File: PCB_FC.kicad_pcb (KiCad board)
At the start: 2 copper layers, 20 parts, among them IC1 STM32F405RGT6, IC2 ICM-42670-P, U1 BMP388, U2 AMS1117-3.3, Y1 X32258MOB4SI

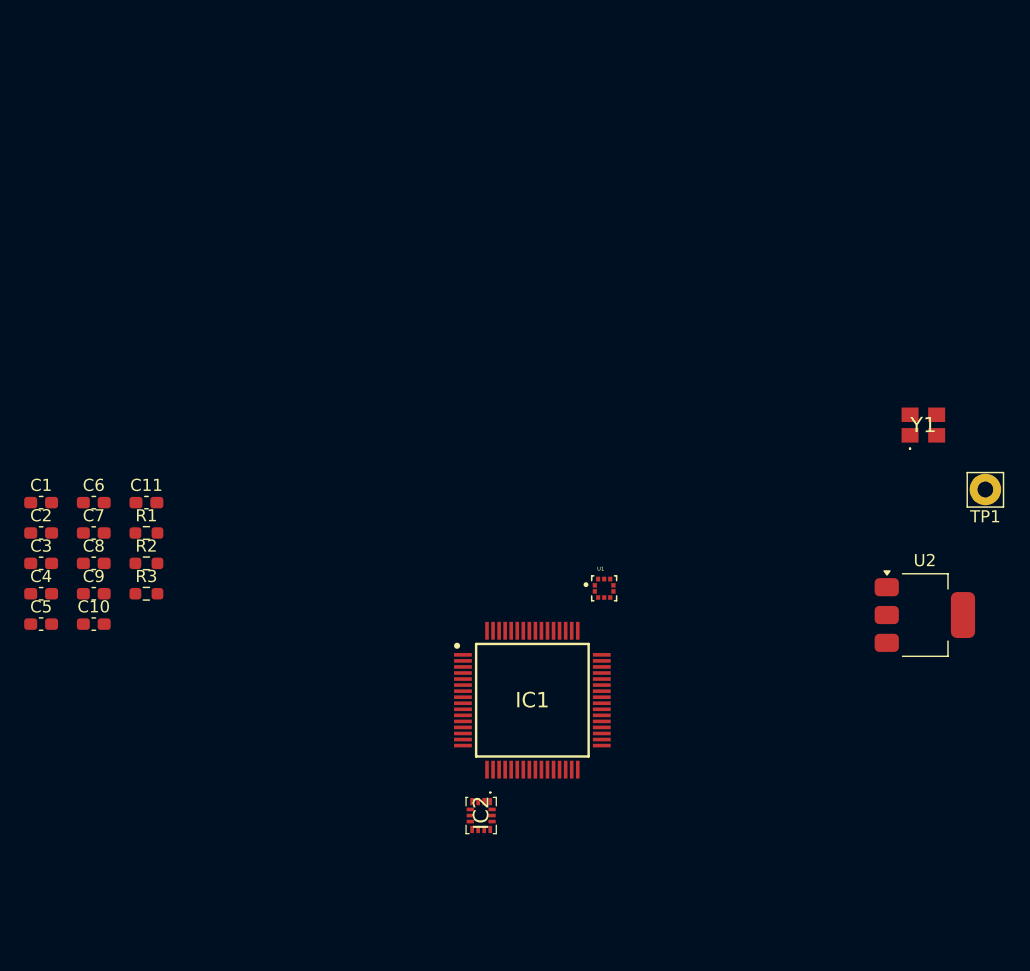
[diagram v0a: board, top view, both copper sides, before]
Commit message: Basic design of schametic done
1. Added folder for library
2. Added USB with termination resistors
3. Added Resistor network for bootstrapping and NRST
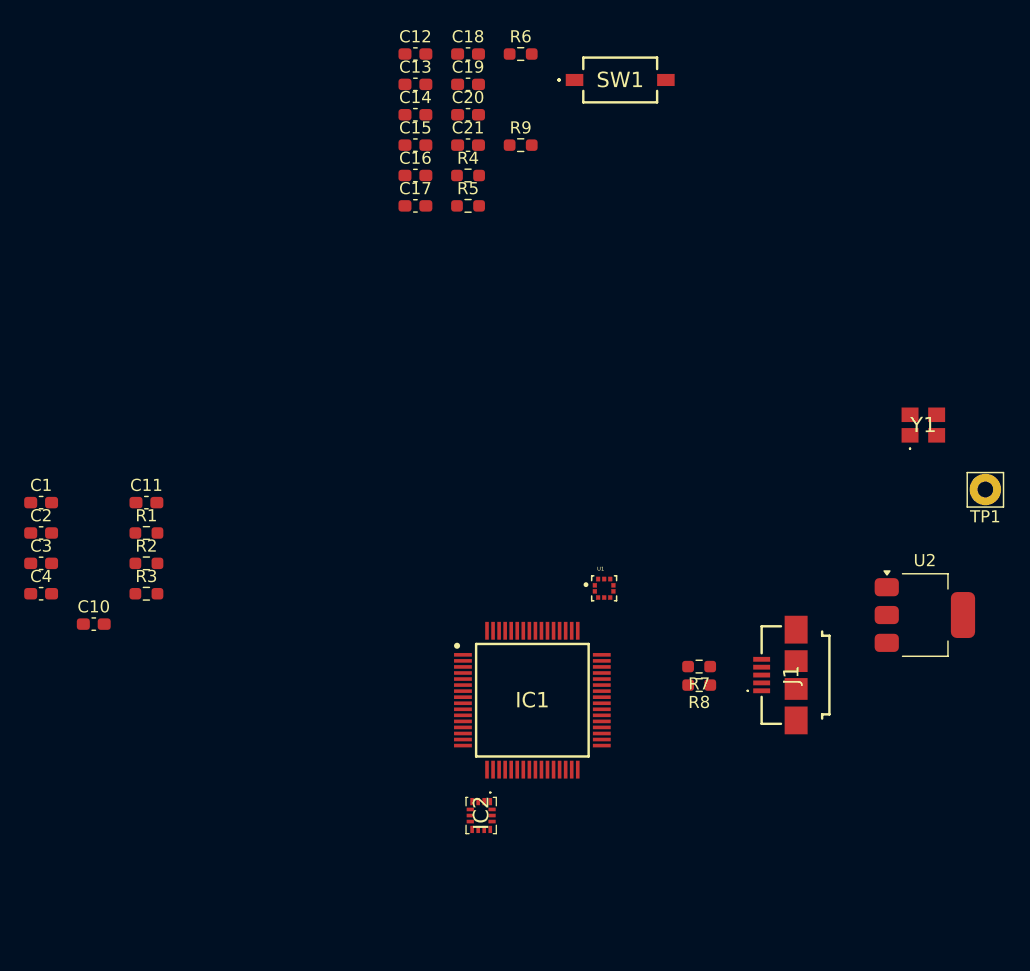
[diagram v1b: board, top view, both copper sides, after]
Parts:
- removed C5, C6: 10pF, Capacitor_SMD:C_0603_1608Metric_Pad1.08x0.95mm_HandSolder
- removed C7, C8, C9: C, Capacitor_SMD:C_0603_1608Metric_Pad1.08x0.95mm_HandSolder
- added C12: 100nf, Capacitor_SMD:C_0603_1608Metric_Pad1.08x0.95mm_HandSolder, F.Cu at (132.8, 47.0)
- added C13: 10uf, Capacitor_SMD:C_0603_1608Metric_Pad1.08x0.95mm_HandSolder, F.Cu at (132.8, 49.5)
- added C14: 10uf, Capacitor_SMD:C_0603_1608Metric_Pad1.08x0.95mm_HandSolder, F.Cu at (132.8, 52.0)
- added C15: 100nf, Capacitor_SMD:C_0603_1608Metric_Pad1.08x0.95mm_HandSolder, F.Cu at (132.8, 54.5)
- added C16: 100nf, Capacitor_SMD:C_0603_1608Metric_Pad1.08x0.95mm_HandSolder, F.Cu at (132.8, 57.0)
- added C17: 100nf, Capacitor_SMD:C_0603_1608Metric_Pad1.08x0.95mm_HandSolder, F.Cu at (132.8, 59.5)
- added C18: 100nf, Capacitor_SMD:C_0603_1608Metric_Pad1.08x0.95mm_HandSolder, F.Cu at (137.1, 47.0)
- added C19: 100nf, Capacitor_SMD:C_0603_1608Metric_Pad1.08x0.95mm_HandSolder, F.Cu at (137.1, 49.5)
- added C20: 100nf, Capacitor_SMD:C_0603_1608Metric_Pad1.08x0.95mm_HandSolder, F.Cu at (137.1, 52.0)
- added C21: 100nf, Capacitor_SMD:C_0603_1608Metric_Pad1.08x0.95mm_HandSolder, F.Cu at (137.1, 54.5)
- added J1: 10104111-0001LF, Footprint:10104111-0001LF, F.Cu at (164.2, 98.3)
- added R4: 4.7k, Resistor_SMD:R_0603_1608Metric_Pad0.98x0.95mm_HandSolder, F.Cu at (137.1, 57.0)
- added R5: 10K, Resistor_SMD:R_0603_1608Metric_Pad0.98x0.95mm_HandSolder, F.Cu at (137.1, 59.5)
- added R6: 10k, Resistor_SMD:R_0603_1608Metric_Pad0.98x0.95mm_HandSolder, F.Cu at (141.5, 47.0)
- added R7: 22R, Resistor_SMD:R_0603_1608Metric_Pad0.98x0.95mm_HandSolder, F.Cu at (156.2, 97.6)
- added R8: 22R, Resistor_SMD:R_0603_1608Metric_Pad0.98x0.95mm_HandSolder, F.Cu at (156.2, 99.2)
- added R9: 1k, Resistor_SMD:R_0603_1608Metric_Pad0.98x0.95mm_HandSolder, F.Cu at (141.5, 54.5)
- added SW1: SW_SPST, Footprint:PTS636SKG25JSMTRLFS, F.Cu at (149.7, 49.1)
- IC1: footprint KiCad:QFP50P1200X1200X160-64N -> Footprint:STM32F405RGT6
- IC2: footprint ICM-42670:ICM42670P -> Footprint:ICM-42670-P
- U1: footprint BMP388:PQFN50P200X200X80-10N -> Footprint:BMP388
- Y1: footprint X225:X32258MOB4SI -> Footprint:X32258MOB4SI
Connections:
- C1 pad 1: /3V3 -> +3.3V
- C1 pad 2: /GND -> GND
- C10 pad 2: /GND -> GND
- C11 pad 2: /GND -> GND
- C2 pad 1: /3V3 -> +3.3V
- C2 pad 2: /GND -> GND
- C3 pad 1: /3V3 -> +3.3V
- C3 pad 2: /GND -> GND
- C4 pad 1: /3V3 -> +3.3V
- C4 pad 2: /GND -> GND
- IC1 pad 12: /GND -> GND
- IC1 pad 13: /VDD -> +3.3V
- IC1 pad 18: /GND -> GND
- IC1 pad 19: /VDD -> +3.3V
- IC1 pad 32: /VDD -> +3.3V
- IC1 pad 44: / OTG_FS_DM -> /OTG_FS_D-
- IC1 pad 45: /OTG_FS_DP -> /OTG_FS_D+
- IC1 pad 46: unconnected-(IC1-PA13-Pad46) -> /SWDIO
- IC1 pad 48: /VDD -> +3.3V
- IC1 pad 49: unconnected-(IC1-PA14-Pad49) -> /SWCLK
- IC1 pad 6: Net-(IC1-PH1) -> /RCC_OUT
- IC1 pad 60: unconnected-(IC1-BOOT0-Pad60) -> Net-(IC1-BOOT0)
- IC1 pad 63: /GND -> GND
- IC1 pad 64: /VDD -> +3.3V
- IC1 pad 7: unconnected-(IC1-NRST-Pad7) -> /NRST
- IC2 pad 5: /3V3 -> +3.3V
- IC2 pad 6: /GND -> unconnected-(IC2-GND-Pad6)
- IC2 pad 8: /3V3 -> +3.3V
- R1 pad 1: /I2C2_SCL -> +3.3V
- R1 pad 2: /3V3 -> /I2C2_SCL
- R2 pad 1: /I2C2_SDA -> +3.3V
- R2 pad 2: /3V3 -> Net-(U1-CSB)
- R3 pad 1: /RCC_OUT -> Net-(Y1-CRYSTAL_1)
- R3 pad 2: Net-(IC1-PH1) -> /RCC_OUT
- U1 pad 1: /3V3 -> +3.3V
- U1 pad 10: /3V3 -> +3.3V
- U1 pad 3: /GND -> GND
- U1 pad 5: /GND -> GND
- U1 pad 6: /PAD -> Net-(U1-CSB)
- U1 pad 8: /GND -> GND
- U1 pad 9: /GND -> GND
- U2 pad 1: /GND -> GND
- U2 pad 2: /3V3 -> +3.3V
- Y1 pad 1: /RCC_IN -> Net-(Y1-CRYSTAL_1)
- Y1 pad 2: unconnected-(Y1-GND_1-Pad2) -> GND
- Y1 pad 3: unconnected-(Y1-CRYSTAL_2-Pad3) -> /RCC_IN
- Y1 pad 4: /GND -> GND

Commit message: Signal routing done
1. Routing for IMU
2. Differentially route pair for USB with termination resistor.
3. HSE crystal oscillator added.
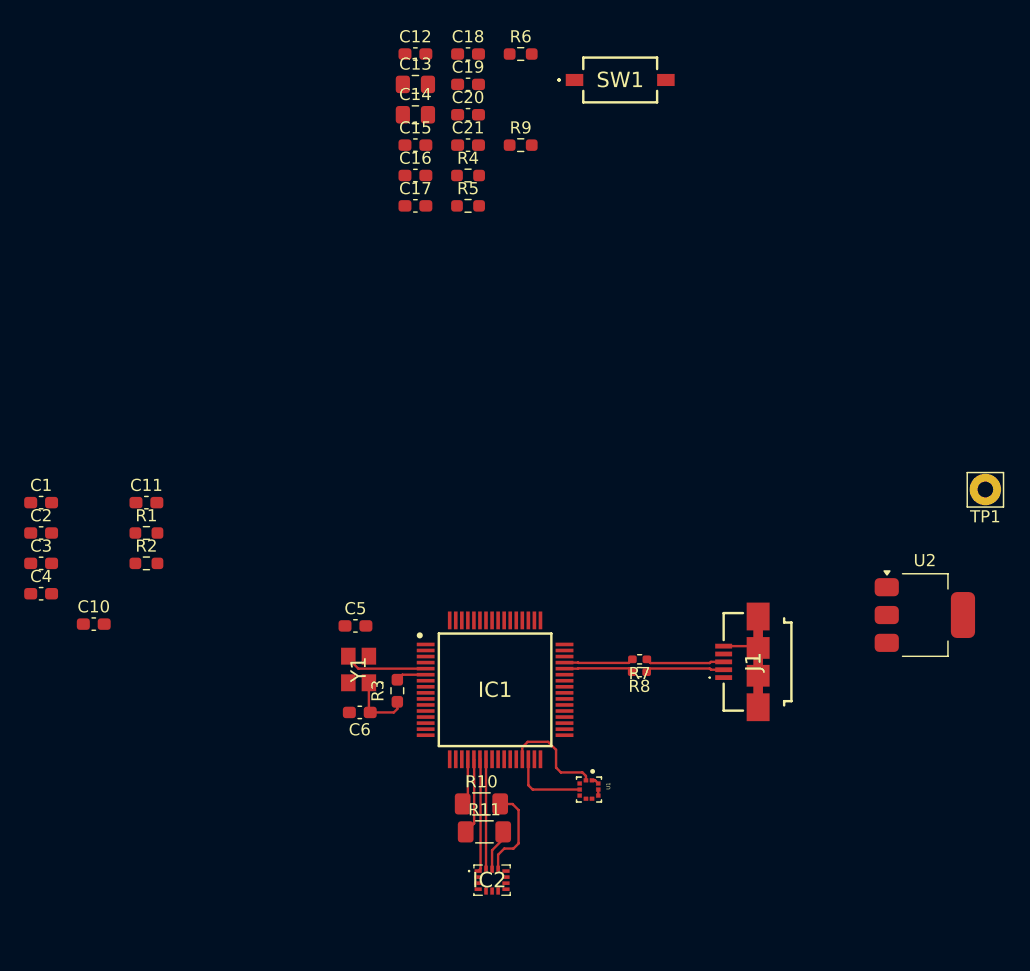
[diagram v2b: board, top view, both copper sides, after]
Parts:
- added C5: C, Capacitor_SMD:C_0603_1608Metric_Pad1.08x0.95mm_HandSolder, F.Cu at (127.8, 94.3)
- added C6: C, Capacitor_SMD:C_0603_1608Metric_Pad1.08x0.95mm_HandSolder, F.Cu at (128.2, 101.4)
- added R10: R, Resistor_SMD:R_1206_3216Metric_Pad1.30x1.75mm_HandSolder, F.Cu at (138.2, 109.0)
- added R11: R, Resistor_SMD:R_1206_3216Metric_Pad1.30x1.75mm_HandSolder, F.Cu at (138.5, 111.3)
- C13, C14: footprint Capacitor_SMD:C_0603_1608Metric_Pad1.08x0.95mm_HandSolder -> Capacitor_SMD:C_0805_2012Metric_Pad1.18x1.45mm_HandSolder
- R7, R8: footprint Resistor_SMD:R_0603_1608Metric_Pad0.98x0.95mm_HandSolder -> Resistor_SMD:R_0402_1005Metric_Pad0.72x0.64mm_HandSolder
- moved Y1 50.9 mm to (128.1, 97.9), turned to 90 degrees
- moved R3 22.2 mm to (131.3, 99.6), turned to 90 degrees
- moved U1 16.7 mm to (147.1, 107.8), turned to -90 degrees
- moved IC2 5.42 mm to (139.1, 115.3), turned to 0 degrees
- moved R8 5.06 mm to (151.3, 98.1)
- moved R7 4.95 mm to (151.3, 97.0)
- moved J1 3.32 mm to (161.1, 97.2)
- moved IC1 3.20 mm to (139.4, 99.5)
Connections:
- IC2 pad 12: /SPI1_CS -> Net-(IC2-AP_CS)
- IC2 pad 13: /SPI1_SCK SPI1 -> Net-(IC2-AP_SCL_/_AP_SCLK)
- IC2 pad 6: unconnected-(IC2-GND-Pad6) -> GND
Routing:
- net GND: track 0.00 -> 10.9 mm
- net /SPI1_MISO SPI1: track 0.00 -> 9.34 mm
- net /SPI1_MOSI SPI1: track 0.00 -> 9.09 mm
- net /I2C2_SCL: track 0.00 -> 8.82 mm
- net Net-(IC2-AP_CS): track 0.00 -> 7.51 mm
- net /RCC_IN: track 0.00 -> 6.94 mm
- net /I2C2_SDA: track 0.00 -> 6.54 mm
- net /D+: track 0.00 -> 6.52 mm
- net /D-: track 0.00 -> 6.50 mm
- net /SPI1_SCK SPI1: track 0.00 -> 6.30 mm
- net /OTG_FS_D+: track 0.00 -> 5.74 mm
- net /OTG_FS_D-: track 0.00 -> 5.71 mm
- net Net-(Y1-CRYSTAL_1): track 0.00 -> 5.44 mm
- net /SPI1_CS: track 0.00 -> 3.87 mm
- net Net-(IC2-AP_SCL_/_AP_SCLK): track 0.00 -> 3.47 mm
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
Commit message: PCB complete add logos
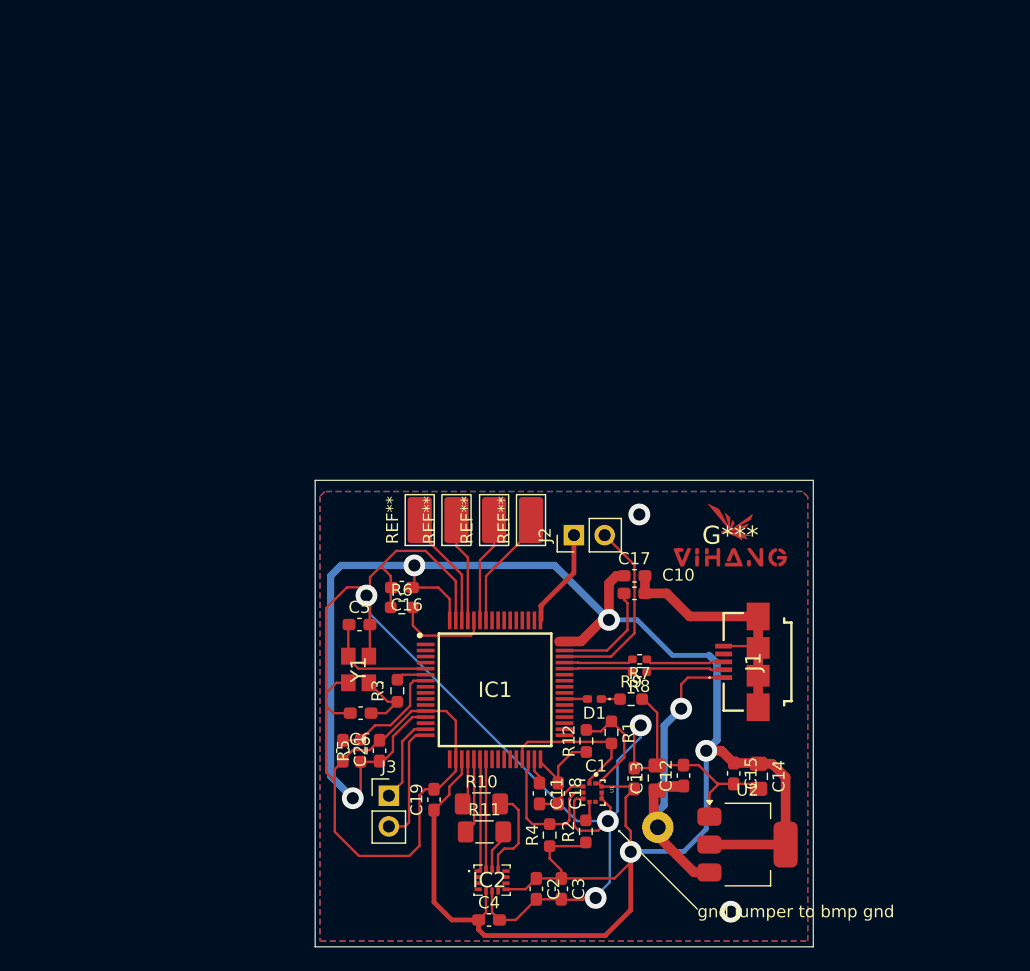
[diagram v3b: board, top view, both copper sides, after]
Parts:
- removed SW1: SW_SPST, Footprint:PTS636SKG25JSMTRLFS
- added D1: LED, LED_SMD:LED_0402_1005Metric_Pad0.77x0.64mm_HandSolder, F.Cu at (147.6, 100.3)
- added G***: LOGO, LOGO, F.Cu at (158.8, 86.8)
- added J2: Conn_01x02, Connector_PinHeader_2.54mm:PinHeader_1x02_P2.54mm_Vertical, F.Cu at (145.9, 86.8)
- added J3: Conn_01x02, Connector_PinHeader_2.54mm:PinHeader_1x02_P2.54mm_Vertical, F.Cu at (130.6, 108.3)
- added R12: 0R, Resistor_SMD:R_0603_1608Metric_Pad0.98x0.95mm_HandSolder, F.Cu at (146.9, 103.8)
- added REF**: TestPoint_Keystone_5019_Miniature, TestPoint:TestPoint_Keystone_5019_Miniature, F.Cu at (133.1, 85.5)
- added REF**: TestPoint_Keystone_5019_Miniature, TestPoint:TestPoint_Keystone_5019_Miniature, F.Cu at (142.3, 85.5)
- added REF**: TestPoint_Keystone_5019_Miniature, TestPoint:TestPoint_Keystone_5019_Miniature, F.Cu at (136.2, 85.5)
- added REF**: TestPoint_Keystone_5019_Miniature, TestPoint:TestPoint_Keystone_5019_Miniature, F.Cu at (139.3, 85.5)
- TP1: moved to B.Cu
- moved C12 63.6 mm to (154.9, 106.6), turned to 90 degrees
- moved C14 61.6 mm to (161.1, 106.7), turned to -90 degrees
- moved C18 61.6 mm to (144.6, 108.1), turned to -90 degrees
- moved C13 60.7 mm to (152.8, 106.8), turned to 90 degrees
- moved C19 59.2 mm to (134.3, 108.6), turned to 90 degrees
- moved C15 58.2 mm to (159.1, 106.5), turned to -90 degrees
- moved R4 54.9 mm to (143.9, 111.5), turned to 90 degrees
- moved C1 54.1 mm to (150.9, 106.9), turned to 90 degrees
- moved C20 53.1 mm to (129.8, 104.6), turned to 90 degrees
- moved C21 51.1 mm to (126.8, 104.6), turned to -90 degrees
- moved C3 50.7 mm to (144.8, 116.0), turned to -90 degrees
- moved C2 50.4 mm to (142.8, 116.0), turned to -90 degrees
- moved R6 46.8 mm to (131.7, 92.7)
- moved R9 46.7 mm to (150.6, 100.3)
- moved R5 45.9 mm to (128.2, 104.6), turned to 90 degrees
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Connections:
- C12 pad 1: Net-(U2-VI) -> +5V
- C13 pad 1: Net-(U2-VI) -> +5V
- C18 pad 1: +3.3V -> Net-(IC1-VDD_2)
- IC1 pad 32: +3.3V -> Net-(IC1-VDD_2)
- TP1 pad 1: Net-(U2-VI) -> +5V
- U2 pad 3: Net-(U2-VI) -> +5V
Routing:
- net +3.3V: track 0.63 -> 208.1 mm, vias 0 -> 5
- net GND: track 10.9 -> 203.2 mm, vias 0 -> 6
- net +5V: track 0.00 -> 30.4 mm, vias 0 -> 1
- net /SWDIO: track 0.00 -> 15.7 mm
- net /USART2_TX: track 0.00 -> 10.1 mm
- net /NRST: track 0.00 -> 9.92 mm
- net /TIM4 PWM(1): track 0.00 -> 9.83 mm
- net /TIM4 PWM(4): track 0.00 -> 9.74 mm
- net /TIM4 PWM(2): track 0.00 -> 9.63 mm
- net Net-(IC1-VCAP_2): track 0.00 -> 9.05 mm
- net /TIM4 PWM(3): track 0.00 -> 8.68 mm
- net /SWCLK: track 0.00 -> 8.18 mm
- net Net-(IC1-BOOT0): track 0.00 -> 8.00 mm
- net /USART2_RX: track 0.00 -> 7.30 mm
- net Net-(IC1-VDD_2): track 0.00 -> 6.86 mm
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- added copper zone on B.Cu, net GND
- added copper zone on F.Cu, net GND
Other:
- board outline added: 41.2 x 38.5 mm
- board text added: "gnd jumper to bmp gnd"
